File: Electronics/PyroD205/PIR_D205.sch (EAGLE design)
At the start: 13 parts, among them IC1 LM324D

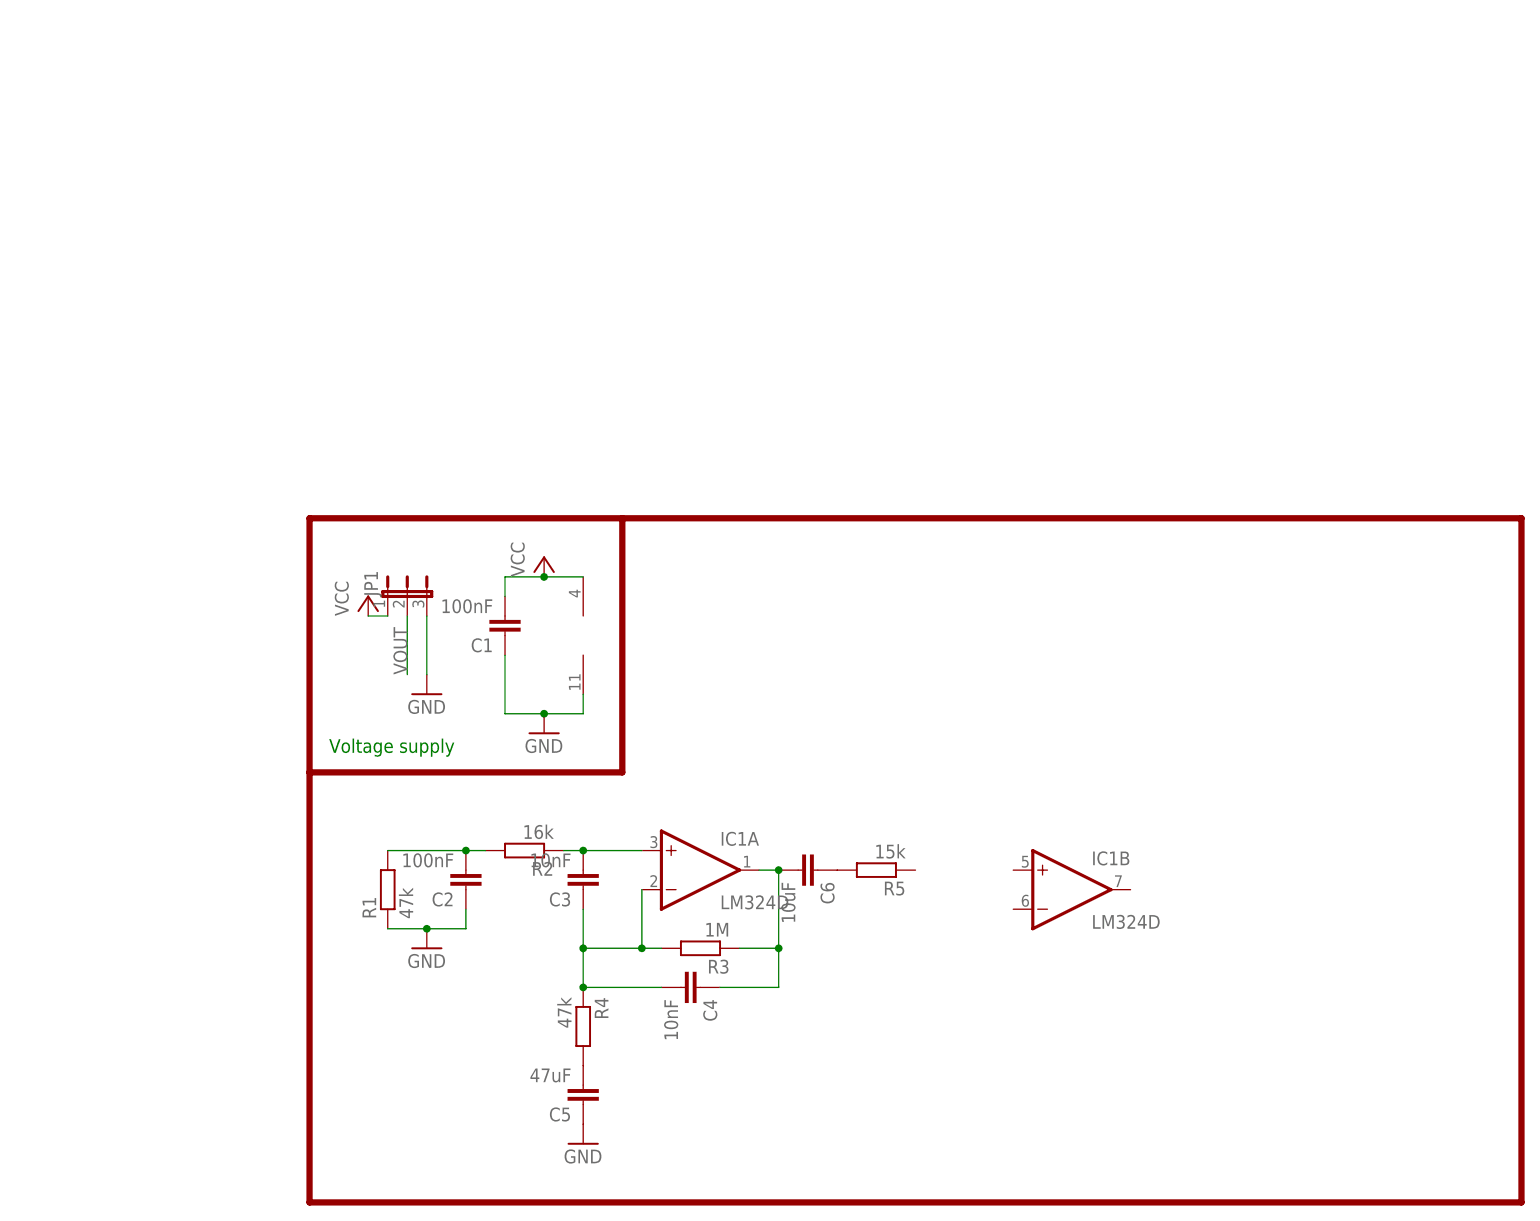
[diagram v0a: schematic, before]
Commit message: finished sensor board for D205B, finished main board Oudini v1.0, Generated Gerbers, modified CAD for PCB support
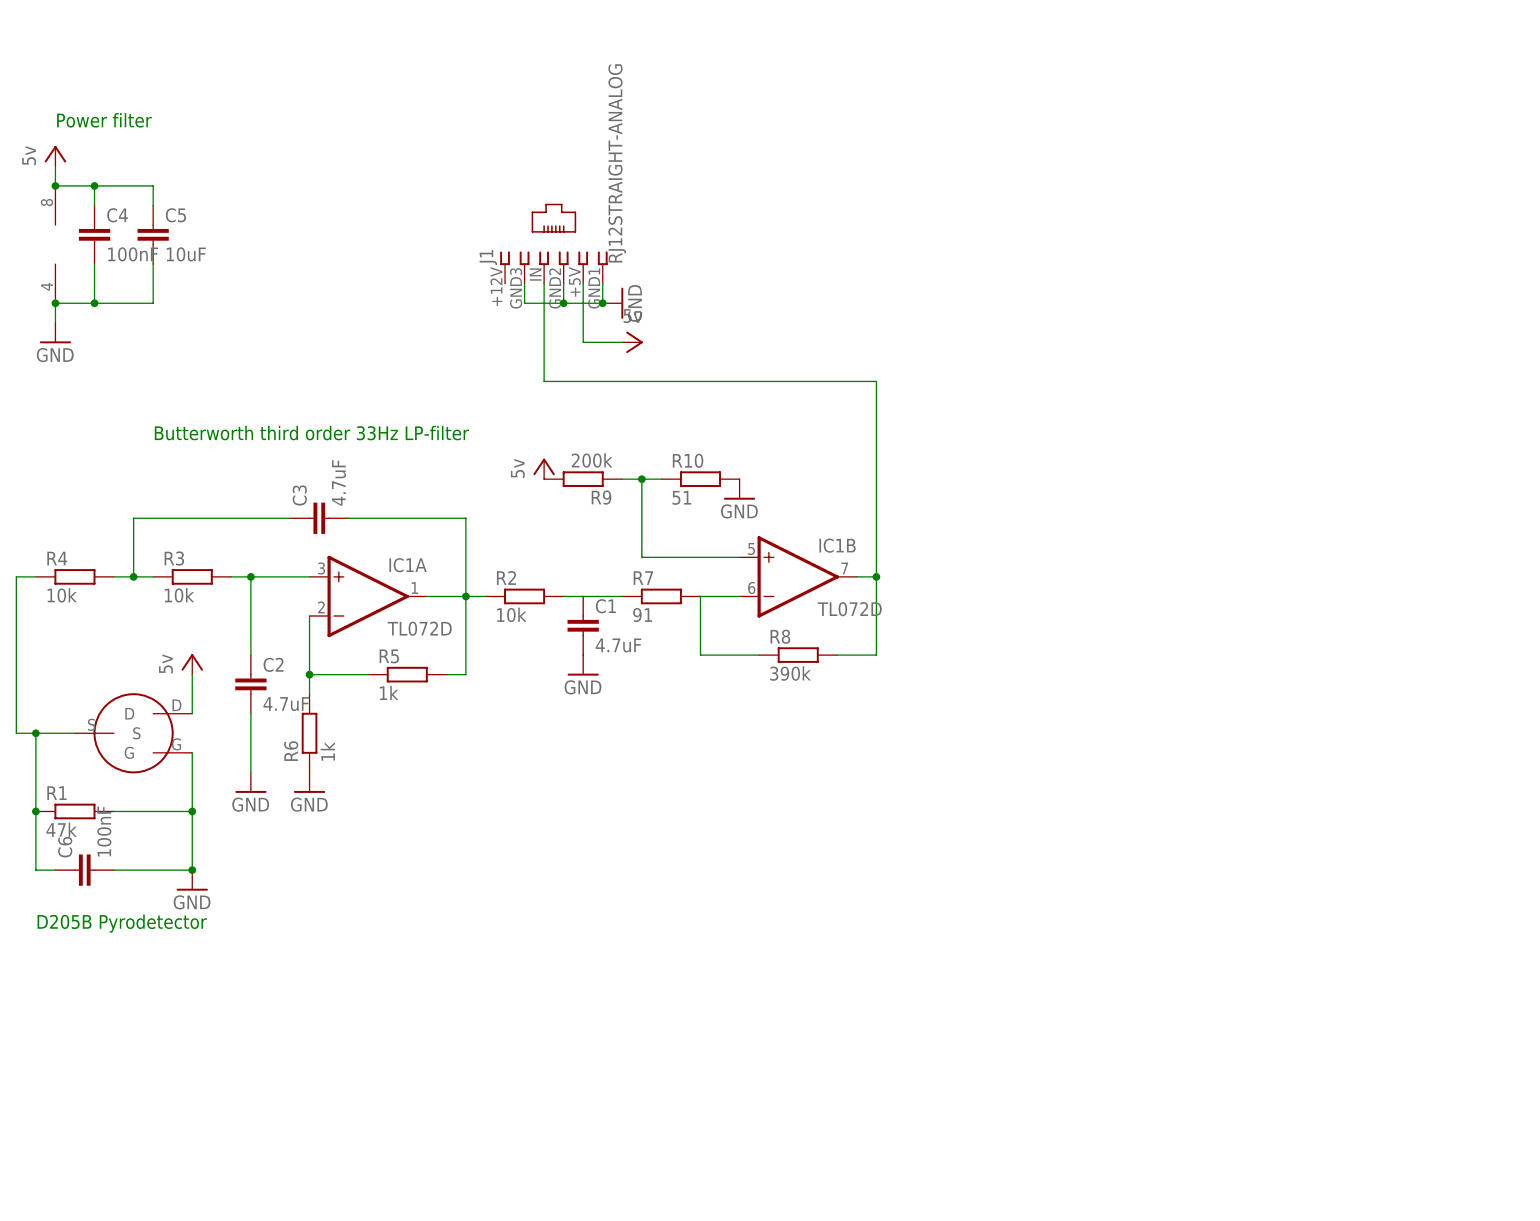
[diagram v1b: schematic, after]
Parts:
- removed JP1: (no value), jumper:JP2E
- added J1: RJ12STRAIGHT-ANALOG, lpatiny:RJ12STRAIGHT-ANALOG
- added R10: 51, resistor:R-EU_R1206
- added R6: 1k, rcl:R-EU_R0805
- added R7: 91, resistor:R-EU_R1206
- added R8: 390k, resistor:R-EU_R1206
- added R9: 200k, resistor:R-EU_R1206
- added U$1: D205B, lpatiny:D205B
- C1, C2: value 100nF -> 4.7uF
- C3: value 10nF -> 4.7uF
- C4: value 10nF -> 100nF
- C5: value 47uF -> 10uF
- C6: value 10uF -> 100nF
- IC1: value LM324D -> TL072D; device linear:LM324D -> linear:TL072D
- R1: device resistor:R-EU_R1206 -> rcl:R-EU_R1206
- R2: value 16k -> 10k; device resistor:R-EU_R1206 -> rcl:R-EU_R0805
- R3: value 1M -> 10k; device resistor:R-EU_R1206 -> rcl:R-EU_R0805
- R4: value 47k -> 10k; device resistor:R-EU_R1206 -> rcl:R-EU_R0805
- R5: value 15k -> 1k; device resistor:R-EU_R1206 -> rcl:R-EU_R0805
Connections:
- removed net VOUT: JP1.2
- new net N$7: IC1B.-IN, R7.2, R8.1
- new net N$8: IC1B.OUT, J1.3, R8.2
- new net N$9: IC1B.+IN, R10.1, R9.1
- net GND: now also C1.2, C2.2, C4.2, C5.2, C6.2, J1.2, J1.4, J1.6, R1.2, R10.2, R6.1, U$1.G; no longer C1.1, C2.1, C5.1, JP1.3, R1.1
- net N$1: now also C6.1, R1.1, R4.1, U$1.S; no longer C2.2, R1.2, R2.2
- net N$2: now also IC1A.OUT, R5.2; no longer IC1A.+IN
- net N$3: now also R5.1, R6.2; no longer C3.1, C4.2, R3.2, R4.1
- net N$4: now also C1.1, R2.2, R7.1; no longer C4.1, C6.2, IC1A.OUT, R3.1
- net N$5: now also C2.1, IC1A.+IN, R3.2; no longer C5.2, R4.2
- net N$6: now also C3.1, R3.1, R4.2; no longer C6.1, R5.2
- net VCC: now also C4.1, C5.1, J1.5, R9.2, U$1.D; no longer C1.2, JP1.1
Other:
- note added: "Butterworth third order 33Hz LP-filter"
- note added: "D205B Pyrodetector"
- note added: "Power filter"
- note removed: "Voltage supply"
- moved on the sheet: C1, C2, C3, C4, C5, C6, IC1A, IC1B, R1, R2, R3, R4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
